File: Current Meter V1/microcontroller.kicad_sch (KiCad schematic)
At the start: 10 parts, among them J401 I2C OLED Display Connector

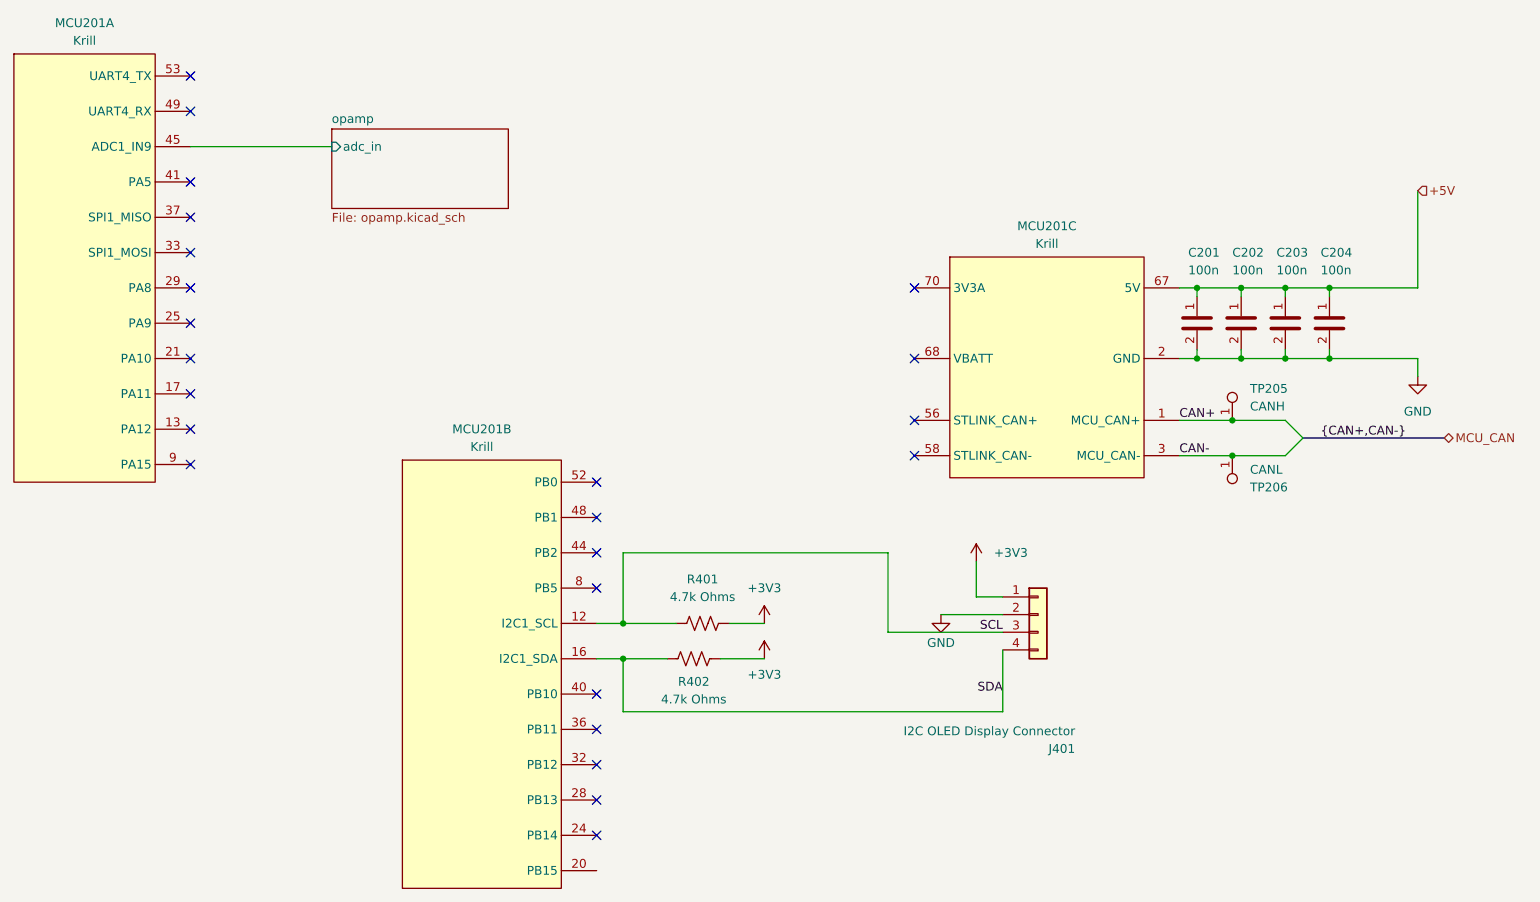
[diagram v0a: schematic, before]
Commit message: sheet organization and microcontroller updated
organized schematic into hierarchical sheets and updated pins on microcontroller
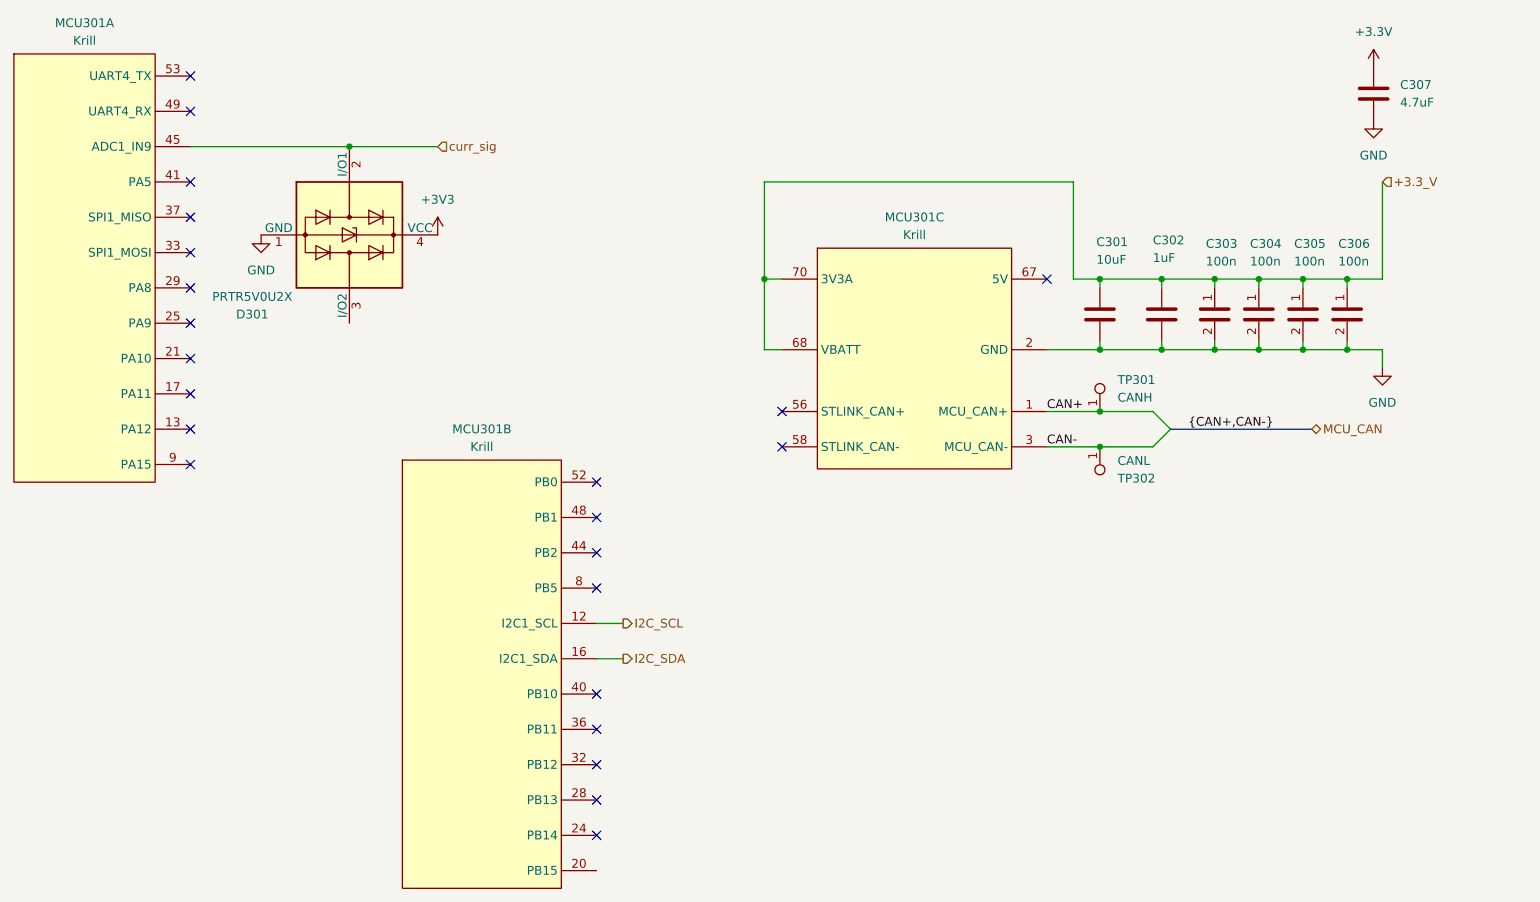
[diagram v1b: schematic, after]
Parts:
- removed J401: I2C OLED Display Connector, symbol Connector_Generic:Conn_01x04
- removed R401, R402: 4.7k Ohms, symbol Device:R_US
- added C301: 10uF, symbol Device:C
- added C302: 1uF, symbol Device:C
- added C307: 4.7uF, symbol Device:C
- added D301: PRTR5V0U2X, Package_TO_SOT_SMD:SOT-143, symbol Power_Protection:PRTR5V0U2X
- renumbered C201 to C303, C202 to C304, C203 to C305, C204 to C306, MCU201 to MCU301, TP205 to TP301, TP206 to TP302
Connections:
- net +3V3: now also D301.4 (VCC)
- net GND: now also C301.2, C302.2, C307.2, D301.1 (GND)
- net +3.3_V: now reaches MCU301.68 (VBATT)
- net +3.3_V: now also C303.1, C304.1, C305.1, C306.1, MCU301.70 (3V3A), MCU301.72 (3V3A), MCU301.74 (3V3A), C301.1, C302.1
- removed net +5V: C303.1, C304.1, C305.1, C306.1, MCU301.67 (5V), MCU301.69 (5V), MCU301.71 (5V)
- net SCL renamed I2C_SCL
- net SDA renamed I2C_SDA
- net opamp/adc_in renamed curr_sig
- net curr_sig: now also D301.2 (I/O1)
- new net: MCU301.67 (5V), MCU301.69 (5V), MCU301.71 (5V)
- new net +3.3V: C307.1
- no-connect marks 24 -> 23
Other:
- removed sheet opamp
- moved on the sheet: C303, C304, C305, C306, MCU301C, TP301, TP302

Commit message: microcontroller
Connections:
- net +5_V: now reaches MCU301.67 (5V), MCU301.69 (5V), MCU301.71 (5V)
- net +5_V: now also C301.1, C302.1, C303.1, C304.1, C305.1, C306.1
- removed net +3.3_V: C301.1, C302.1, C303.1, C304.1, C305.1, C306.1, MCU301.68 (VBATT), MCU301.70 (3V3A), MCU301.72 (3V3A), MCU301.74 (3V3A)
- new net: MCU301.70 (3V3A), MCU301.72 (3V3A), MCU301.74 (3V3A)
- no-connect marks 23 -> 24
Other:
- moved on the sheet: C301, C302, C303, C304, C305, C306

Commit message: microcontroller update
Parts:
- removed D301: PRTR5V0U2X, Package_TO_SOT_SMD:SOT-143, symbol Power_Protection:PRTR5V0U2X
- renumbered C306 to C301, C305 to C302, C304 to C303, C303 to C304, C302 to C305, C301 to C306
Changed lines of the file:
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@@
-	)
-	(junction
-		(at 111.76 67.31)
-		(diameter 0)
-		(color 0 0 0 0)
 	)
 	(junction
@@
 	(wire
 		(pts
-			(xy 111.76 67.31) (xy 124.46 67.31)
+			(xy 88.9 67.31) (xy 124.46 67.31)
 		)
 		(stroke
@@
 		(pts
 			(xy 256.54 95.25) (xy 256.54 96.52)
-		)
-		(stroke
-			(width 0)
-			(type default)
-		)
-	)
-	(wire
-		(pts
-			(xy 88.9 67.31) (xy 111.76 67.31)
 		)
 		(stroke
@@
 		(dnp no)
 		(fields_autoplaced yes)
-		(property "Reference" "#PWR0305"
+		(property "Reference" "#PWR0302"
 			(at 259.08 69.85 0)
 			(effects
@@
 			(project "CMU - Current Measurement Unit"
 				(path "/a2a38fd0-928e-4aba-88ec-c7bc808fdbf7/70482173-e24b-439b-8681-bded10c38af4"
-					(reference "#PWR0305")
+					(reference "#PWR0302")
 					(unit 1)
 				)
@@
 		(on_board yes)
 		(dnp no)
-		(property "Reference" "C304"
+		(property "Reference" "C303"
 			(at 236.22 81.28 0)
 			(effects
@@
 			(project "CMU - Current Measurement Unit"
 				(path "/a2a38fd0-928e-4aba-88ec-c7bc808fdbf7/70482173-e24b-439b-8681-bded10c38af4"
-					(reference "C304")
+					(reference "C303")
 					(unit 1)
 				)
@@
 	)
 	(symbol
-		(lib_id "power:GND")
-		(at 99.06 80.01 0)
-		(unit 1)
-		(exclude_from_sim no)
-		(in_bom yes)
-		(on_board yes)
-		(dnp no)
-		(fields_autoplaced yes)
-		(property "Reference" "#PWR0301"
-			(at 99.06 86.36 0)
-			(effects
-				(font
-					(size 1.27 1.27)
-				)
-				(hide yes)
-			)
-		)
-		(property "Value" "GND"
-			(at 99.06 85.09 0)
-			(effects
-				(font
-					(size 1.27 1.27)
-				)
-			)
-		)
-		(property "Footprint" ""
-			(at 99.06 80.01 0)
-			(effects
-				(font
-					(size 1.27 1.27)
-				)
-				(hide yes)
-			)
-		)
-		(property "Datasheet" ""
-			(at 99.06 80.01 0)
-			(effects
-				(font
-					(size 1.27 1.27)
-				)
-				(hide yes)
-			)
-		)
-		(property "Description" "Power symbol creates a global label with name \"GND\" , ground"
-			(at 99.06 80.01 0)
-			(effects
-				(font
-					(size 1.27 1.27)
-				)
-				(hide yes)
-			)
-		)
-		(pin "1"
-		)
-		(instances
-			(project "CMU - Current Measurement Unit"
-				(path "/a2a38fd0-928e-4aba-88ec-c7bc808fdbf7/70482173-e24b-439b-8681-bded10c38af4"
-					(reference "#PWR0301")
-					(unit 1)
-				)
-			)
-		)
-	)
-	(symbol
-		(lib_id "power:+3V3")
-		(at 124.46 80.01 0)
-		(unit 1)
-		(exclude_from_sim no)
-		(in_bom yes)
-		(on_board yes)
-		(dnp no)
-		(fields_autoplaced yes)
-		(property "Reference" "#PWR0302"
-			(at 124.46 83.82 0)
-			(effects
-				(font
-					(size 1.27 1.27)
-				)
-				(hide yes)
-			)
-		)
-		(property "Value" "+3V3"
-			(at 124.46 74.93 0)
-			(effects
-				(font
-					(size 1.27 1.27)
-				)
-			)
-		)
-		(property "Footprint" ""
-			(at 124.46 80.01 0)
-			(effects
-				(font
-					(size 1.27 1.27)
-				)
-				(hide yes)
-			)
-		)
-		(property "Datasheet" ""
-			(at 124.46 80.01 0)
-			(effects
-				(font
-					(size 1.27 1.27)
-				)
-				(hide yes)
-			)
-		)
-		(property "Description" "Power symbol creates a global label with name \"+3V3\""
-			(at 124.46 80.01 0)
-			(effects
-				(font
-					(size 1.27 1.27)
-				)
-				(hide yes)
-			)
-		)
-		(pin "1"
-		)
-		(instances
-			(project "CMU - Current Measurement Unit"
-				(path "/a2a38fd0-928e-4aba-88ec-c7bc808fdbf7/70482173-e24b-439b-8681-bded10c38af4"
-					(reference "#PWR0302")
-					(unit 1)
-				)
-			)
-		)
-	)
-	(symbol
 		(lib_id "Device:C")
 		(at 259.08 59.69 0)
@@
 		(dnp no)
 		(fields_autoplaced yes)
-		(property "Reference" "#PWR0304"
+		(property "Reference" "#PWR0301"
 			(at 259.08 59.69 0)
 			(effects
@@
 			(project "CMU - Current Measurement Unit"
 				(path "/a2a38fd0-928e-4aba-88ec-c7bc808fdbf7/70482173-e24b-439b-8681-bded10c38af4"
-					(reference "#PWR0304")
+					(reference "#PWR0301")
 					(unit 1)
 				)
@@
 		(on_board yes)
 		(dnp no)
-		(property "Reference" "C306"
+		(property "Reference" "C301"
 			(at 223.52 81.28 0)
 			(effects
@@
 			(project "CMU - Current Measurement Unit"
 				(path "/a2a38fd0-928e-4aba-88ec-c7bc808fdbf7/70482173-e24b-439b-8681-bded10c38af4"
-					(reference "C306")
+					(reference "C301")
 					(unit 1)
 				)
@@
 		(on_board yes)
 		(dnp no)
-		(property "Reference" "C305"
+		(property "Reference" "C302"
 			(at 229.87 81.28 0)
 			(effects
@@
 			(project "CMU - Current Measurement Unit"
 				(path "/a2a38fd0-928e-4aba-88ec-c7bc808fdbf7/70482173-e24b-439b-8681-bded10c38af4"
-					(reference "C305")
+					(reference "C302")
 					(unit 1)
 				)
@@
 		(on_board yes)
 		(dnp no)
-		(property "Reference" "C303"
+		(property "Reference" "C304"
 			(at 242.57 81.28 0)
 			(effects
@@
 			(project "CMU - Current Measurement Unit"
 				(path "/a2a38fd0-928e-4aba-88ec-c7bc808fdbf7/70482173-e24b-439b-8681-bded10c38af4"
-					(reference "C303")
+					(reference "C304")
 					(unit 1)
 				)
@@
 	)
 	(symbol
-		(lib_id "Power_Protection:PRTR5V0U2X")
-		(at 111.76 80.01 270)
-		(unit 1)
-		(exclude_from_sim no)
-		(in_bom yes)
-		(on_board yes)
-		(dnp no)
-		(property "Reference" "D301"
-			(at 97.79 91.44 90)
-			(effects
-				(font
-					(size 1.27 1.27)
-				)
-			)
-		)
-		(property "Value" "PRTR5V0U2X"
-			(at 97.79 88.9 90)
-			(effects
-				(font
-					(size 1.27 1.27)
-				)
-			)
-		)
-		(property "Footprint" "Package_TO_SOT_SMD:SOT-143"
-			(at 111.76 81.534 0)
-			(effects
-				(font
-					(size 1.27 1.27)
-				)
-				(hide yes)
-			)
-		)
-		(property "Datasheet" "https://assets.nexperia.com/documents/data-sheet/PRTR5V0U2X.pdf"
-			(at 111.76 81.534 0)
-			(effects
-				(font
-					(size 1.27 1.27)
-				)
-				(hide yes)
-			)
-		)
-		(property "Description" "Ultra low capacitance double rail-to-rail ESD protection diode, SOT-143"
-			(at 111.76 80.01 0)
-			(effects
-				(font
-					(size 1.27 1.27)
-				)
-				(hide yes)
-			)
-		)
-		(pin "2"
-		)
-		(pin "1"
-		)
-		(pin "3"
-		)
-		(pin "4"
-		)
-		(instances
-			(project "CMU - Current Measurement Unit"
-				(path "/a2a38fd0-928e-4aba-88ec-c7bc808fdbf7/70482173-e24b-439b-8681-bded10c38af4"
-					(reference "D301")
-					(unit 1)
-				)
-			)
-		)
-	)
-	(symbol
 		(lib_id "bfr_microcontrollers:Krill")
 		(at 130.81 128.27 0)
@@
 		(on_board yes)
 		(dnp no)
-		(property "Reference" "C301"
+		(property "Reference" "C306"
 			(at 257.048 81.026 0)
 			(effects
@@
 			(project "CMU - Current Measurement Unit"
 				(path "/a2a38fd0-928e-4aba-88ec-c7bc808fdbf7/70482173-e24b-439b-8681-bded10c38af4"
-					(reference "C301")
+					(reference "C306")
 					(unit 1)
 				)
@@
 		(on_board yes)
 		(dnp no)
-		(property "Reference" "C302"
+		(property "Reference" "C305"
 			(at 250.19 80.772 0)
 			(effects
@@
 			(project "CMU - Current Measurement Unit"
 				(path "/a2a38fd0-928e-4aba-88ec-c7bc808fdbf7/70482173-e24b-439b-8681-bded10c38af4"
-					(reference "C302")
+					(reference "C305")
 					(unit 1)
 				)

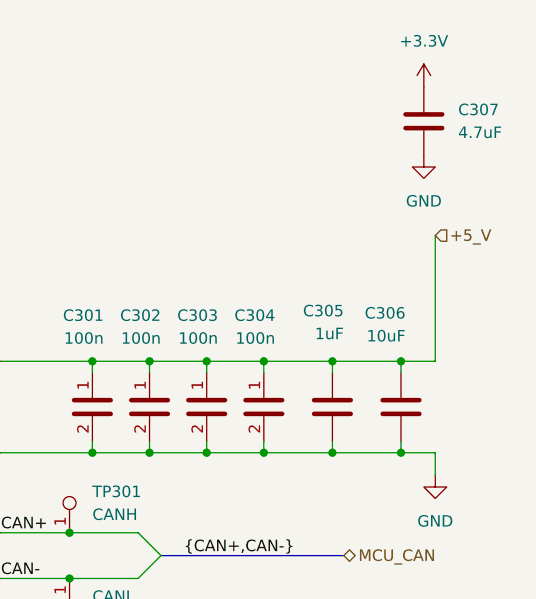
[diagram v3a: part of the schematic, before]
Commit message: updated footprints
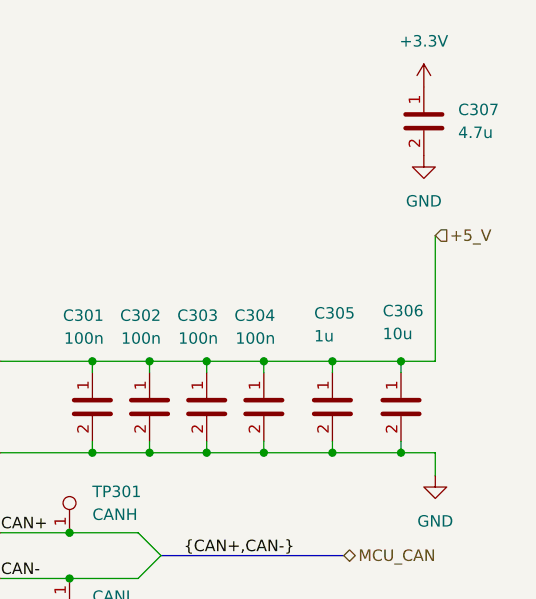
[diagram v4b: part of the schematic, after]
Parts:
- removed C305: 1uF, symbol Device:C
- removed C306: 10uF, symbol Device:C
- removed C307: 4.7uF, symbol Device:C
- added C305: 1u, Capacitor_SMD:C_0603_1608Metric_Pad1.08x0.95mm_HandSolder, symbol bfr_capacitors:CL10A105KB8NNNC
- added C306: 10u, Capacitor_SMD:C_0805_2012Metric_Pad1.18x1.45mm_HandSolder, symbol bfr_capacitors:KGM21AR71A106KU
- added C307: 4.7u, Capacitor_SMD:C_0805_2012Metric_Pad1.18x1.45mm_HandSolder, symbol bfr_capacitors:KGM21AR51A475KU
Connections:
- net +3.3V: now also C307.1
- net +5_V: now also C305.1, C306.1
- net GND: now also C305.2, C306.2, C307.2

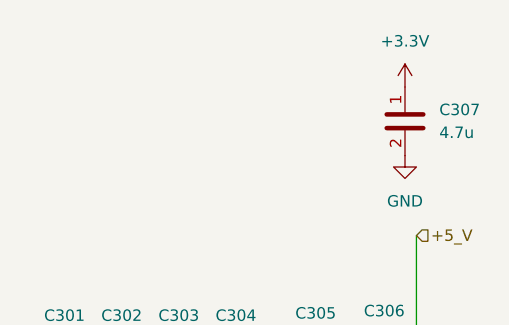
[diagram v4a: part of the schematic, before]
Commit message: updated layout
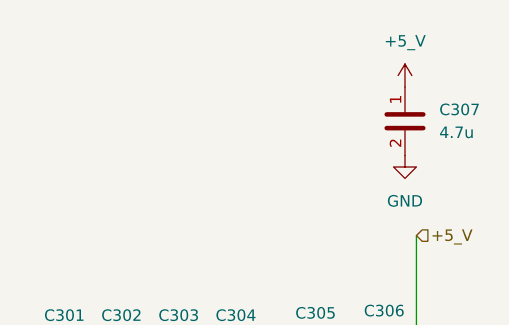
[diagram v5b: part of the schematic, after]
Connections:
- net +3.3V is gone; now on net +5_V: C307.1
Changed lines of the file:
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@@
 			)
 		)
-		(property "Value" "+3.3V"
+		(property "Value" "+5_V"
 			(at 259.08 50.8 0)
 			(effects
